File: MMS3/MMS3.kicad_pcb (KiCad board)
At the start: 4 copper layers, 100 x 50 mm, 198 parts, among them J1 86093488324755V1LF, J2 AMASS XT60, J3 Programming header, J7 AMASS XT60, J8 RJ45_LED_Shielded, J800 USB_C_Receptacle_USB2.0_16P, J9 RJ45_LED_Shielded, Q700 MMST3904, SW3 TC-6615Z-12.5-260, SW4 SK12D07VG5, SW5 TC-6615Z-12.5-260, U1 STM32F405RGTx, U15 AMS1117-3.3, U2 TPS54560BDDA, U302 CH334P, U4 TPD2EUSB30DRTR-TP, U401 TPD2EUSB30DRTR-TP, U5 TPD2EUSB30DRTR-TP, U500 TJA1044GTK_3Z, U501 TJA1044GTK_3Z, U6 AT24C256C, U700 STM32F103CBTx, U801 FSUSB42UMX, U802 FSUSB42UMX, X1 X32258MOB4SI, X2 Q13FC1350000400, Y700 Crystal_GND24, Y900 Crystal_GND24

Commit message: initial PCB update
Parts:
- removed C21, C22, C23, C25, C26, C312, C313, C701, C702, C703, C704, C705, C706, C800, C900: 100nF, PCM_JLCPCB:C_0402
- removed C24: 10uF, PCM_JLCPCB:C_0603
- removed C28, C29: 33pF, PCM_JLCPCB:C_0402
- removed C30, C31, C32, C33, C34: 10uF, PCM_JLCPCB:C_0805
- removed C7: 10nF, PCM_JLCPCB:C_0402
- removed C700, C904: 1uF, PCM_JLCPCB:C_0402
- removed C8: 18pF, PCM_JLCPCB:C_0402
- removed C902: 10uF, PCM_JLCPCB:C_0402
- removed D301, D700, D701: Red, PCM_JLCPCB:D_0603
- removed FB401: ~, PCM_JLCPCB:FB_0603
- removed J800: USB_C_Receptacle_USB2.0_16P, Connector_USB:USB_C_Receptacle_GCT_USB4105-xx-A_16P_TopMnt_Horizontal
- removed LED1: FixLed307, FixLed307:FixLed307
- removed Q700: MMST3904, Package_TO_SOT_SMD:SOT-23
- removed R27, R308, R31, R40: 1kΩ, PCM_JLCPCB:R_0402
- removed R500, R701, R703, R705, R706, R709, R802, R804, R805, R807: 10kΩ, PCM_JLCPCB:R_0402
- removed R700, R702: 100kΩ, PCM_JLCPCB:R_0402
- removed R704, R708, R715, R716, R902, R903, R906, R907: 22Ω, PCM_JLCPCB:R_0402
- removed R707, R713: 220Ω, PCM_JLCPCB:R_0402
- removed R710, R714: 100Ω, PCM_JLCPCB:R_0402
- removed R711: 24.9kΩ, PCM_JLCPCB:R_0402
- removed R712: 1.5kΩ, PCM_JLCPCB:R_0402
- removed R803, R806: 22kΩ, PCM_JLCPCB:R_0402
- removed REF**: WEEE-Logo_4.2x6mm_SilkScreen, Symbol:WEEE-Logo_4.2x6mm_SilkScreen
- removed SW3, SW5: TC-6615Z-12.5-260, Tact-sw:SW-TH_4P-L7.3-TC-6615Z-12.5-260
- removed SW4: SK12D07VG5, Slide-SW:SW-TH_SK12D07VG5-1
- removed TP10, TP11, TP12, TP13, TP14, TP5, TP7, TP8, TP9: TestPoint, TestPoint:TestPoint_Pad_D1.0mm
- removed U302: CH334P, Package_DFN_QFN:QFN-16-1EP_3x3mm_P0.5mm_EP1.7x1.7mm
- removed U401: TPD2EUSB30DRTR-TP, Package_TO_SOT_SMD:SOT-723
- removed U500: TJA1044GTK_3Z, Package_SON:HVSON-8-1EP_3x3mm_P0.65mm_EP1.6x2.4mm
- removed U700: STM32F103CBTx, Package_QFP:LQFP-48_7x7mm_P0.5mm
- removed U801, U802: FSUSB42UMX, Package_DFN_QFN:UQFN-10_1.4x1.8mm_P0.4mm
- removed X2: Q13FC1350000400, PCM_JLCPCB:FC-135R_L3.2-W1.5
- removed Y700: Crystal_GND24, PCM_JLCPCB:CRYSTAL-SMD_4P-L3.2-W2.5-BL
- removed Y900: Crystal_GND24, Crystal:Crystal_SMD_3225-4Pin_3.2x2.5mm
- added C14: 10nF, PCM_JLCPCB:C_0402, F.Cu at (152.4, 154.4)
- added C48: 22uF, PCM_JLCPCB:C_0805, F.Cu at (139.2, 166.7)
- added C51: 22uF, PCM_JLCPCB:C_0805, F.Cu at (139.2, 169.7)
- added C64: 100uF, Capacitor_SMD:CP_Elec_10x10, F.Cu at (130.6, 149.4)
- added D10: SS510B, PCM_JLCPCB:D_SMB, F.Cu at (141.6, 151.8)
- added D2: SMF58CA, PCM_JLCPCB:D_SOD-123FL, F.Cu at (139.8, 163.5)
- added D7: SS510B, PCM_JLCPCB:D_SMB, F.Cu at (141.6, 146.3)
- added D8: Red, PCM_JLCPCB:D_0603, F.Cu at (139.4, 155.9)
- added D9: Red, PCM_JLCPCB:D_0603, F.Cu at (139.4, 158.5)
- added J4: USB_C_Receptacle_USB2.0_16P, Connector_USB:USB_C_Receptacle_GCT_USB4105-xx-A_16P_TopMnt_Horizontal, F.Cu at (153.6, 148.8)
- added J5: USB_PD, Connector_USB:USB_C_Receptacle_GCT_USB4105-xx-A_16P_TopMnt_Horizontal, F.Cu at (129.1, 167.1)
- added Q1: MMBT5401 200-300, PCM_JLCPCB:Q_SOT-23, F.Cu at (146.9, 168.7)
- added Q2: DOINGTER DON50N10-TL, CMSA160N10:PDFN-8_L5.8-W5.0-P1.27-LS6.1-BL, F.Cu at (157.1, 176.9)
- added Q3: DOINGTER DON50N10-TL, CMSA160N10:PDFN-8_L5.8-W5.0-P1.27-LS6.1-BL, F.Cu at (148.2, 176.9)
- added S1: Tactile Button, 160gf, PCM_JLCPCB:SW_TS-1088-AR02016, F.Cu at (148.0, 164.0)
- added S2: Tactile Button, 160gf, PCM_JLCPCB:SW_TS-1088-AR02016, F.Cu at (157.1, 164.0)
- added S3: Tactile Button, 160gf, PCM_JLCPCB:SW_TS-1088-AR02016, F.Cu at (157.1, 168.5)
- added U3: TPD2EUSB30DRTR-TP, Package_TO_SOT_SMD:SOT-723, F.Cu at (149.6, 154.9)
- added U7: MX74502D23_C41433189, MX74502D23:UDFN-8L_L2.0-W3.0-P0.50-BL-EP, F.Cu at (143.4, 156.9)
- C10, C11: value 22pF -> 100nF; footprint PCM_JLCPCB:C_0402 -> PCM_JLCPCB:C_0603
- C12, C13: footprint PCM_JLCPCB:C_0402 -> PCM_JLCPCB:C_0603
- C16: value 2.2uF -> 100nF; footprint PCM_JLCPCB:C_0402 -> PCM_JLCPCB:C_0603
- C17: value 2.2uF -> 1uF; footprint PCM_JLCPCB:C_0402 -> PCM_JLCPCB:C_0603
- C18: value 4.7nF -> 22uF; footprint PCM_JLCPCB:C_0402 -> PCM_JLCPCB:C_0805
- C19: value 100nF -> 100uF; footprint PCM_JLCPCB:C_0402 -> Capacitor_SMD:CP_Elec_10x10
- C3, C5: value 100nF -> 12pF; footprint PCM_JLCPCB:C_0402 -> PCM_JLCPCB:C_0603
- C36, C37: footprint PCM_JLCPCB:C_0402 -> PCM_JLCPCB:C_0805
- C38, C39: value 220nF -> 10uF
- C40: value 100nF -> 10uF
- C41, C42: value 22uF -> 220nF
- C45: value 22uF -> 100nF
- C50: value 100uF -> 22uF; footprint Capacitor_SMD:CP_Elec_10x10 -> PCM_JLCPCB:C_0805
- C9: value 18pF -> 100nF; footprint PCM_JLCPCB:C_0402 -> PCM_JLCPCB:C_0603
- D1: value SMF58CA -> Red; footprint PCM_JLCPCB:D_SOD-123FL -> PCM_JLCPCB:D_0603
- D4: value SS510B -> Red; footprint PCM_JLCPCB:D_SMB -> PCM_JLCPCB:D_0603
- J3: value Programming header -> WCH Link; footprint Connector_PinHeader_1.27mm:PinHeader_1x06_P1.27mm_Vertical -> Connector_PinSocket_2.54mm:PinSocket_2x05_P2.54mm_Vertical
- R10: footprint PCM_JLCPCB:R_0402 -> PCM_JLCPCB:R_0603
- R11: value 1kΩ -> 10kΩ; footprint PCM_JLCPCB:R_0402 -> PCM_JLCPCB:R_0603
- R12, R13: value 100Ω -> 1kΩ; footprint PCM_JLCPCB:R_0402 -> PCM_JLCPCB:R_0603
- R14: value 10kΩ -> 33kΩ
- R15: value 10kΩ -> 39kΩ; footprint PCM_JLCPCB:R_0402 -> PCM_JLCPCB:R_0603
- R16: value 22Ω -> 12kΩ; footprint PCM_JLCPCB:R_0402 -> PCM_JLCPCB:R_0603
- R17: value 22Ω -> 4.7kΩ; footprint PCM_JLCPCB:R_0402 -> PCM_JLCPCB:R_0603
- R18: value 22Ω -> 1kΩ; footprint PCM_JLCPCB:R_0402 -> PCM_JLCPCB:R_0603
- R19: value 22Ω -> 47kΩ; footprint PCM_JLCPCB:R_0402 -> PCM_JLCPCB:R_0603
- R20: value 22Ω -> 18kΩ; footprint PCM_JLCPCB:R_0402 -> PCM_JLCPCB:R_0603
- R21: value 22Ω -> 5.1kΩ; footprint PCM_JLCPCB:R_0402 -> PCM_JLCPCB:R_0603
- R22: value 100Ω -> 5.1kΩ; footprint PCM_JLCPCB:R_0402 -> PCM_JLCPCB:R_0603
- R7: value 33kΩ -> 10kΩ
- R8: value 5.1kΩ -> 1.5kΩ; footprint PCM_JLCPCB:R_0402 -> PCM_JLCPCB:R_0603
- R9: value 5.1kΩ -> 1kΩ; footprint PCM_JLCPCB:R_0402 -> PCM_JLCPCB:R_0603
- U1: value STM32F405RGTx -> CH32L103C8T6_C22398291; footprint Package_QFP:LQFP-64_10x10mm_P0.5mm -> CH32L103C8T6:LQFP-48_L7.0-W7.0-P0.50-LS9.0-BL
- X1: value X32258MOB4SI -> X322525MOB4SI
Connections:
- net /CAN_TR1/CAN.+ renamed /MMS_CONNECTOR_DOWNSTREAM/CAN1.+
- net /CAN_TR1/CAN.- renamed /MMS_CONNECTOR_DOWNSTREAM/CAN1.-
- C10 pad 1: /MCU/OSC_HSI_IN -> +3V3
- C11 pad 1: /MCU/OSC_HSI_OUT -> +3V3
- C12 pad 1: Net-(U1-NRST) -> +3V3
- C15 pad 1: /MCU/VDDA -> /USB_Data/VBUS
- C16 pad 1: Net-(U1-VCAP_1) -> BRD_VIN
- C17 pad 1: Net-(U1-VCAP_2) -> BRD_VIN
- C17 pad 2: GND -> Net-(U7-VCAP)
- C18 pad 1: /MCU/BOOT0 -> /PSU/NMos1/D
- C19 pad 1: +3V3 -> +5V
- C20 pad 1: +3V3 -> BRD_VIN
- C3 pad 1: +3V3 -> GND
- C3 pad 2: GND -> /CH32L103_Wrapper/CH32L103/OSC_IN
- C35 pad 1: /VRM/Cap_protec -> BRD_VIN
- C35 pad 2: GND -> /PSU/Buck Converter/Cap_protec
- C36 pad 1: /MCU/VDDA -> /PSU/Buck Converter/Cap_protec
- C37 pad 1: +3V3 -> BRD_VIN
- C37 pad 2: GND -> /PSU/Buck Converter/Cap_protec
- C38 pad 1: BRD_VIN -> /PSU/Buck Converter/Cap_protec
- C38 pad 2: /VRM/Cap_protec -> GND
- C39 pad 1: /VRM/Cap_protec -> BRD_VIN
- C39 pad 2: GND -> /PSU/Buck Converter/Cap_protec
- C40 pad 1: Net-(U2-SW) -> /PSU/Buck Converter/Cap_protec
- C40 pad 2: Net-(U2-BOOT) -> GND
- C41 pad 1: Net-(C41-Pad1) -> BRD_VIN
- C41 pad 2: GND -> /PSU/Buck Converter/Cap_protec
- C42 pad 1: Net-(C41-Pad1) -> /PSU/Buck Converter/Cap_protec
- C45 pad 1: Net-(C41-Pad1) -> Net-(U2-SW)
- C45 pad 2: GND -> Net-(U2-BOOT)
- C46 pad 1: Net-(C41-Pad1) -> /PSU/Buck Converter/5V out
- C47 pad 1: Net-(C41-Pad1) -> /PSU/Buck Converter/5V out
- C5 pad 2: +5V -> /CH32L103_Wrapper/CH32L103/OSC_Out
- C50 pad 1: +5V -> /PSU/Buck Converter/5V out
- C9 pad 1: /MCU/OSC32_OUT -> +3V3
- D1 pad 1: BRD_VIN -> Net-(D1-Pad1)
- D1 pad 2: GND -> /CH32L103_Wrapper/CH32L103/UART1.TX
- D4 pad 1: +5V -> /CH32L103_Wrapper/Chainbus_addr3
- D4 pad 2: Net-(C41-Pad1) -> Net-(D4-Pad2)
- D5 pad 2: VBUS -> /USB_Data/VBUS
- D6 pad 1: Net-(D6-Pad1) -> /CH32L103_Wrapper/PC13
- D6 pad 2: /Slide-SW/SEL -> Net-(D6-Pad2)
- J1 pad b1: /Interboard_connector/Chainbus_addr3 -> /CH32L103_Wrapper/Chainbus_addr3
- J1 pad b10: /I2C_Flash/I2C_Memory.SCL -> /CH32L103_Wrapper/I2C2.SCL
- J1 pad b11: /Interboard_connector/Chainbus.CS -> /CH32L103_Wrapper/SPI2.CS
- J1 pad b12: /Interboard_connector/Chainbus.SCK -> /CH32L103_Wrapper/SPI2.SCK
- J1 pad b13: /Interboard_connector/Chainbus.MOSI -> /CH32L103_Wrapper/SPI2.MOSI
- J1 pad b14: /Interboard_connector/Chainbus.MISO -> /CH32L103_Wrapper/SPI2.MISO
- J1 pad b15: /Interboard_connector/Chainbus.RX -> /CH32L103_Wrapper/UART4.RX
- J1 pad b16: /Interboard_connector/Chainbus.TX -> /CH32L103_Wrapper/UART4.TX
- J1 pad b2: /Interboard_connector/Chainbus_addr4 -> /CH32L103_Wrapper/Chainbus_addr4
- J1 pad b3: /Interboard_connector/Chainbus_addr0 -> /CH32L103_Wrapper/Chainbus_addr0
- J1 pad b4: /Interboard_connector/Chainbus_addr1 -> /CH32L103_Wrapper/Chainbus_addr1
- J1 pad b5: /Interboard_connector/Chainbus_addr2 -> /CH32L103_Wrapper/Chainbus_addr2
- J1 pad b6: /Interboard_connector/Chainbus_addr5 -> /CH32L103_Wrapper/Chainbus_addr5
- J1 pad b7: /Interboard_connector/Chainbus_addr6 -> /CH32L103_Wrapper/Chainbus_addr6
- J1 pad b8: /Interboard_connector/Chainbus_addr7 -> /CH32L103_Wrapper/Chainbus_addr7
- J1 pad b9: /I2C_Flash/I2C_Memory.SDA -> /CH32L103_Wrapper/I2C2.SDA
- J3 pad 1: +3V3 -> /CH32L103_Wrapper/CH32L103/UART1.TX
- J3 pad 2: /STlink-BMprobe/DIO -> /CH32L103_Wrapper/CH32L103/PA14 (SWCLK)
- J3 pad 3: /STlink-BMprobe/CLK -> /CH32L103_Wrapper/CH32L103/UART1.RX
- J3 pad 4: /STlink-BMprobe/STLINK-RST -> /CH32L103_Wrapper/CH32L103/PA13 (SWDIO)
- J3 pad 5: GND -> unconnected-(J3-Pin_5-Pad5)
- J3 pad 6: /STlink-BMprobe/STLINK-BOOT0 -> GND
- J9 pad 7: /MMS_CONNECTOR_UPSTREAM/USB_MMS_CONN.D- -> /MMS_CONNECTOR_DOWNSTREAM/USB_MMS_CONN.D-
- J9 pad 8: /MMS_CONNECTOR_UPSTREAM/USB_MMS_CONN.D+ -> /MMS_CONNECTOR_DOWNSTREAM/USB_MMS_CONN.D+
- L1 pad 2: Net-(C41-Pad1) -> /PSU/Buck Converter/5V out
- R1 pad 2: /MCU/USER_LED_2 -> /TXD2_LED
- R10 pad 1: /MCU/BOOT0 -> /CH32L103_Wrapper/CH32L103/BOOT0
- R11 pad 1: /MCU/BOOT_EN -> /CH32L103_Wrapper/CH32L103/~{RST}
- R11 pad 2: /MCU/BOOT0 -> +3V3
- R12 pad 1: /MCU/NRST -> Net-(D4-Pad2)
- R12 pad 2: /MCU/SWD.~{RST} -> GND
- R13 pad 1: /MCU/USR_BTN -> Net-(D6-Pad2)
- R13 pad 2: /MCU/USR_BUTTON -> GND
- R14 pad 1: /MCU/USR_BTN -> Net-(J4-SHIELD)
- R14 pad 2: +3V3 -> GND
- R15 pad 1: /MCU/NRST -> BRD_VIN
- R15 pad 2: +3V3 -> /PSU/EN
- R16 pad 1: /USB HUB/USBIN1_R.D+ -> /PSU/EN
- R16 pad 2: /USB HUB/USBIN1.D+ -> GND
- R17 pad 1: /USB HUB/USBIN1_R.D- -> Net-(D8-Pad1)
- R17 pad 2: /USB HUB/USBIN1.D- -> GND
- R18 pad 1: /USB HUB/USBBYP.D+ -> Net-(D9-Pad1)
- R18 pad 2: /USB HUB/USBIN1.D+ -> GND
- R19 pad 1: /USB HUB/USBBYP.D- -> BRD_VIN
- R19 pad 2: /USB HUB/USBIN1.D- -> Net-(U7-OV)
- R20 pad 1: /USB HUB/USBBYP.D- -> Net-(U7-OV)
- R20 pad 2: /MCU/USB_MCU.D- -> GND
- R21 pad 1: /USB HUB/USBBYP.D+ -> /CH32L103_Wrapper/CH32L103/I2C1.SDA
- R21 pad 2: /MCU/USB_MCU.D+ -> GND
- R22 pad 1: /MCU/NRST -> /CH32L103_Wrapper/CH32L103/I2C1.SCL
- R22 pad 2: Net-(U1-NRST) -> GND
- R33 pad 2: /VRM/Cap_protec -> /PSU/Buck Converter/Cap_protec
- R34 pad 1: /VRM/Cap_protec -> /PSU/Buck Converter/Cap_protec
- R36 pad 1: Net-(C41-Pad1) -> /PSU/Buck Converter/5V out
- R4 pad 2: /MCU/USER_LED_1 -> /RXD2_LED
- R7 pad 1: Net-(J800-SHIELD) -> /CH32L103_Wrapper/CH32L103/UART1.RX
- R8 pad 1: /USBC_CONN/CC2 -> /CH32L103_Wrapper/PC13
- R8 pad 2: GND -> Net-(Q1-B)
- R9 pad 1: /USBC_CONN/CC1 -> Net-(D1-Pad1)
- TP1 pad 1: /CAN_TR1/CAN.TX -> /CAN_TR2/CAN.RX
- TP19 pad 1: Net-(C41-Pad1) -> /PSU/Buck Converter/5V out
- TP3 pad 1: /CAN_TR1/CAN.RX -> /CAN_TR2/CAN.TX
- U1 pad 10: /Interboard_connector/Altmode14 -> /CH32L103_Wrapper/Chainbus_addr3
- U1 pad 11: /Interboard_connector/Altmode15 -> /CH32L103_Wrapper/Chainbus_addr4
- U1 pad 12: GND -> /CH32L103_Wrapper/Chainbus_addr0
- U1 pad 13: /MCU/VDDA -> /CH32L103_Wrapper/Chainbus_addr1
- U1 pad 14: /Interboard_connector/Altmode7 -> /CH32L103_Wrapper/Chainbus_addr2
- U1 pad 15: /Interboard_connector/Altmode8 -> /CH32L103_Wrapper/Chainbus_addr5
- U1 pad 16: /Interboard_connector/Altmode9 -> /CH32L103_Wrapper/Chainbus_addr6
- U1 pad 17: /Interboard_connector/Altmode10 -> /CH32L103_Wrapper/Chainbus_addr7
- U1 pad 18: GND -> /CH32L103_Wrapper/UART4.TX
- U1 pad 19: +3V3 -> /CH32L103_Wrapper/UART4.RX
- U1 pad 2: unconnected-(U1-PC13-Pad2) -> /CH32L103_Wrapper/PC13
- U1 pad 20: /MCU/BOOT_EN -> /TXD2_LED
- U1 pad 21: /Interboard_connector/Chainbus_addr2 -> /CH32L103_Wrapper/I2C2.SDA
- U1 pad 22: /Interboard_connector/Chainbus_addr1 -> /CH32L103_Wrapper/I2C2.SCL
- U1 pad 23: /Interboard_connector/Chainbus_addr0 -> GND
- U1 pad 24: /Interboard_connector/Altmode16 -> +3V3
- U1 pad 25: /MCU/USER_LED_3 -> /CH32L103_Wrapper/SPI2.CS
- U1 pad 26: /MCU/USER_LED_2 -> /CH32L103_Wrapper/SPI2.SCK
- U1 pad 27: /MCU/USER_LED_1 -> /CH32L103_Wrapper/SPI2.MOSI
- U1 pad 28: unconnected-(U1-PB2-Pad28) -> /CH32L103_Wrapper/SPI2.MISO
- U1 pad 29: /I2C_Flash/I2C_Memory.SCL -> /CH32L103_Wrapper/CH32L103/PA8
- U1 pad 3: /MCU/OSC32_IN -> /CH32L103_Wrapper/CH32L103/PC14 (OSC32)
- U1 pad 30: /I2C_Flash/I2C_Memory.SDA -> /CH32L103_Wrapper/CH32L103/UART1.TX
- U1 pad 31: Net-(U1-VCAP_1) -> /CH32L103_Wrapper/CH32L103/UART1.RX
- U1 pad 32: +3V3 -> /CH32L103_Wrapper/USB1.D-
- U1 pad 33: /CAN_TR2/CAN.RX -> /CH32L103_Wrapper/USB1.D+
- U1 pad 34: /Interboard_connector/Altmode4 -> /CH32L103_Wrapper/CH32L103/PA13 (SWDIO)
- U1 pad 35: /Interboard_connector/Altmode5 -> GND
- U1 pad 36: /Interboard_connector/Altmode6 -> +3V3
- U1 pad 37: /Interboard_connector/Chainbus_addr5 -> /CH32L103_Wrapper/CH32L103/PA14 (SWCLK)
- U1 pad 38: /Interboard_connector/Chainbus_addr6 -> /CH32L103_Wrapper/CH32L103/PA15
- U1 pad 39: /Interboard_connector/Chainbus_addr7 -> /CH32L103_Wrapper/CH32L103/PB3
- U1 pad 4: /MCU/OSC32_OUT -> /CH32L103_Wrapper/CH32L103/PC15 (OSC32)
- U1 pad 40: /Interboard_connector/Chainbus_addr3 -> /CH32L103_Wrapper/CH32L103/PB4
- U1 pad 41: /Interboard_connector/Altmode1 -> /CH32L103_Wrapper/CH32L103/PB5
- U1 pad 42: /Interboard_connector/Altmode2 -> /CH32L103_Wrapper/CH32L103/I2C1.SCL
- U1 pad 43: /Interboard_connector/Altmode3 -> /CH32L103_Wrapper/CH32L103/I2C1.SDA
- U1 pad 44: /MCU/USB_MCU.D- -> /CH32L103_Wrapper/CH32L103/BOOT0
- U1 pad 45: /MCU/USB_MCU.D+ -> /CAN_TR2/CAN.RX
- U1 pad 46: /MCU/SWD.SWDIO -> /CAN_TR2/CAN.TX
- U1 pad 47: Net-(U1-VCAP_2) -> GND
- U1 pad 5: /MCU/OSC_HSI_IN -> /CH32L103_Wrapper/CH32L103/OSC_IN
- U1 pad 6: /MCU/OSC_HSI_OUT -> /CH32L103_Wrapper/CH32L103/OSC_Out
- U1 pad 7: Net-(U1-NRST) -> /CH32L103_Wrapper/CH32L103/~{RST}
- U1 pad 8: /Interboard_connector/Altmode12 -> GND
- U1 pad 9: /Interboard_connector/Altmode13 -> +3V3
- U5 pad 1: /MMS_CONNECTOR_UPSTREAM/USB_MMS_CONN.D- -> /MMS_CONNECTOR_DOWNSTREAM/USB_MMS_CONN.D-
- U5 pad 2: /MMS_CONNECTOR_UPSTREAM/USB_MMS_CONN.D+ -> /MMS_CONNECTOR_DOWNSTREAM/USB_MMS_CONN.D+
- U6 pad 5: /I2C_Flash/I2C_Memory.SDA -> /CH32L103_Wrapper/I2C2.SDA
- U6 pad 6: /I2C_Flash/I2C_Memory.SCL -> /CH32L103_Wrapper/I2C2.SCL
- X1 pad 1: /MCU/OSC_HSI_OUT -> /CH32L103_Wrapper/CH32L103/OSC_IN
- X1 pad 3: /MCU/OSC_HSI_IN -> /CH32L103_Wrapper/CH32L103/OSC_Out
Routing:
- net (no net): track 0.00 -> 311.8 mm, vias 0 -> 11
- net /MCU/SWD.SWDIO: track 58.0 -> 0.00 mm, vias 2 -> 0
- net /Slide-SW/SEL: track 54.3 -> 0.00 mm, vias 1 -> 0
- net +3V3: track 318.1 -> 370.6 mm, vias 49 -> 50
- net /Interboard_connector/Chainbus.SCK: track 49.0 -> 0.00 mm, vias 1 -> 0
- net /CH32L103_Wrapper/SPI2.SCK: track 0.00 -> 49.0 mm, vias 0 -> 1
- net /Interboard_connector/Chainbus.MISO: track 39.8 -> 0.00 mm, vias 1 -> 0
- net /CH32L103_Wrapper/SPI2.MISO: track 0.00 -> 39.8 mm, vias 0 -> 1
- net /Interboard_connector/Chainbus.TX: track 31.6 -> 0.00 mm, vias 1 -> 0
- net /CH32L103_Wrapper/UART4.TX: track 0.00 -> 31.6 mm, vias 0 -> 1
- net /Interboard_connector/Chainbus_addr3: track 27.9 -> 0.00 mm, vias 1 -> 0
- net /CH32L103_Wrapper/Chainbus_addr3: track 0.00 -> 27.9 mm, vias 0 -> 1
- net /USB switch1/USB_OUT2.D-: track 27.0 -> 0.00 mm
- net /USB switch1/USB_OUT2.D+: track 26.5 -> 0.00 mm
- net /Interboard_connector/Chainbus.CS: track 26.3 -> 0.00 mm, vias 1 -> 0
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- added copper zone on In2.Cu, net /CH32L103_Wrapper/Chainbus_addr1
- added copper zone on F.Cu, net /PSU/Buck Converter/5V out
- added copper zone on F.Cu, net /USB_Data/VBUS
- added copper zone on In2.Cu, net /USB_Data/VBUS
- removed copper zone on In2.Cu, net /MCU/VDDA
- removed copper zone on F.Cu, net /VRM/Cap_protec
- removed copper zone on F.Cu, net Net-(C41-Pad1)
- removed copper zone on F.Cu, net VBUS
- removed copper zone on In2.Cu, net VBUS

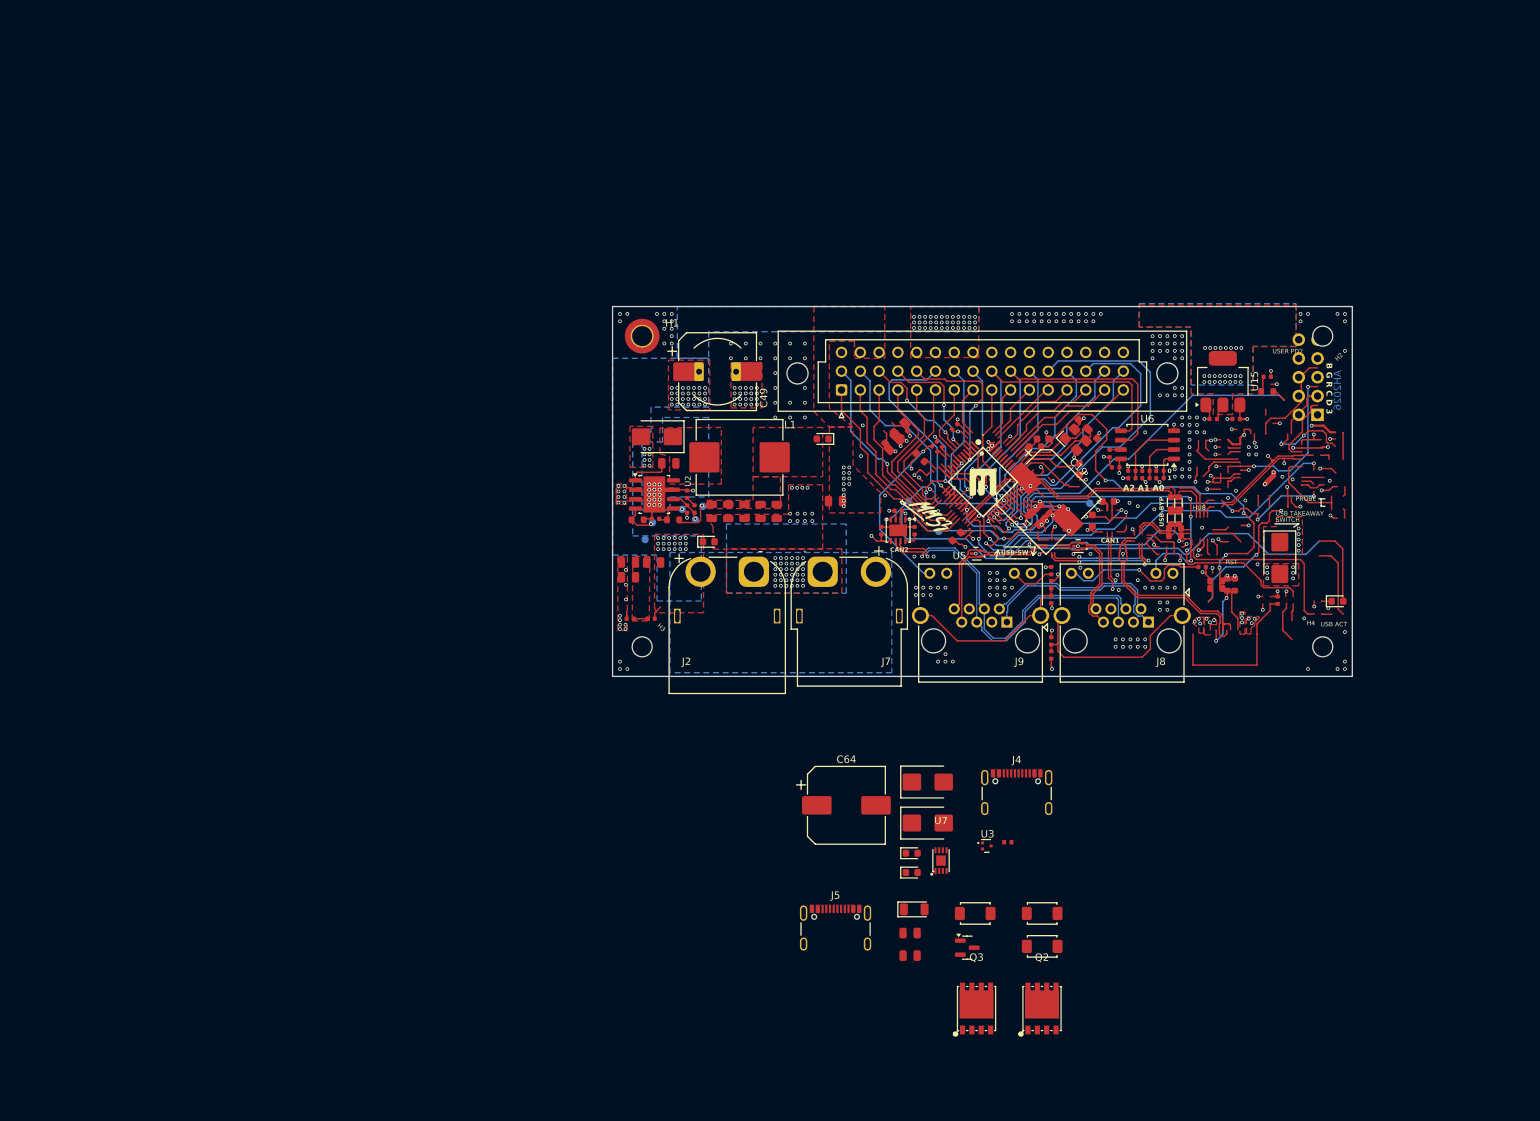
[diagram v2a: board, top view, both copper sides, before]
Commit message: re-added onboard programmer
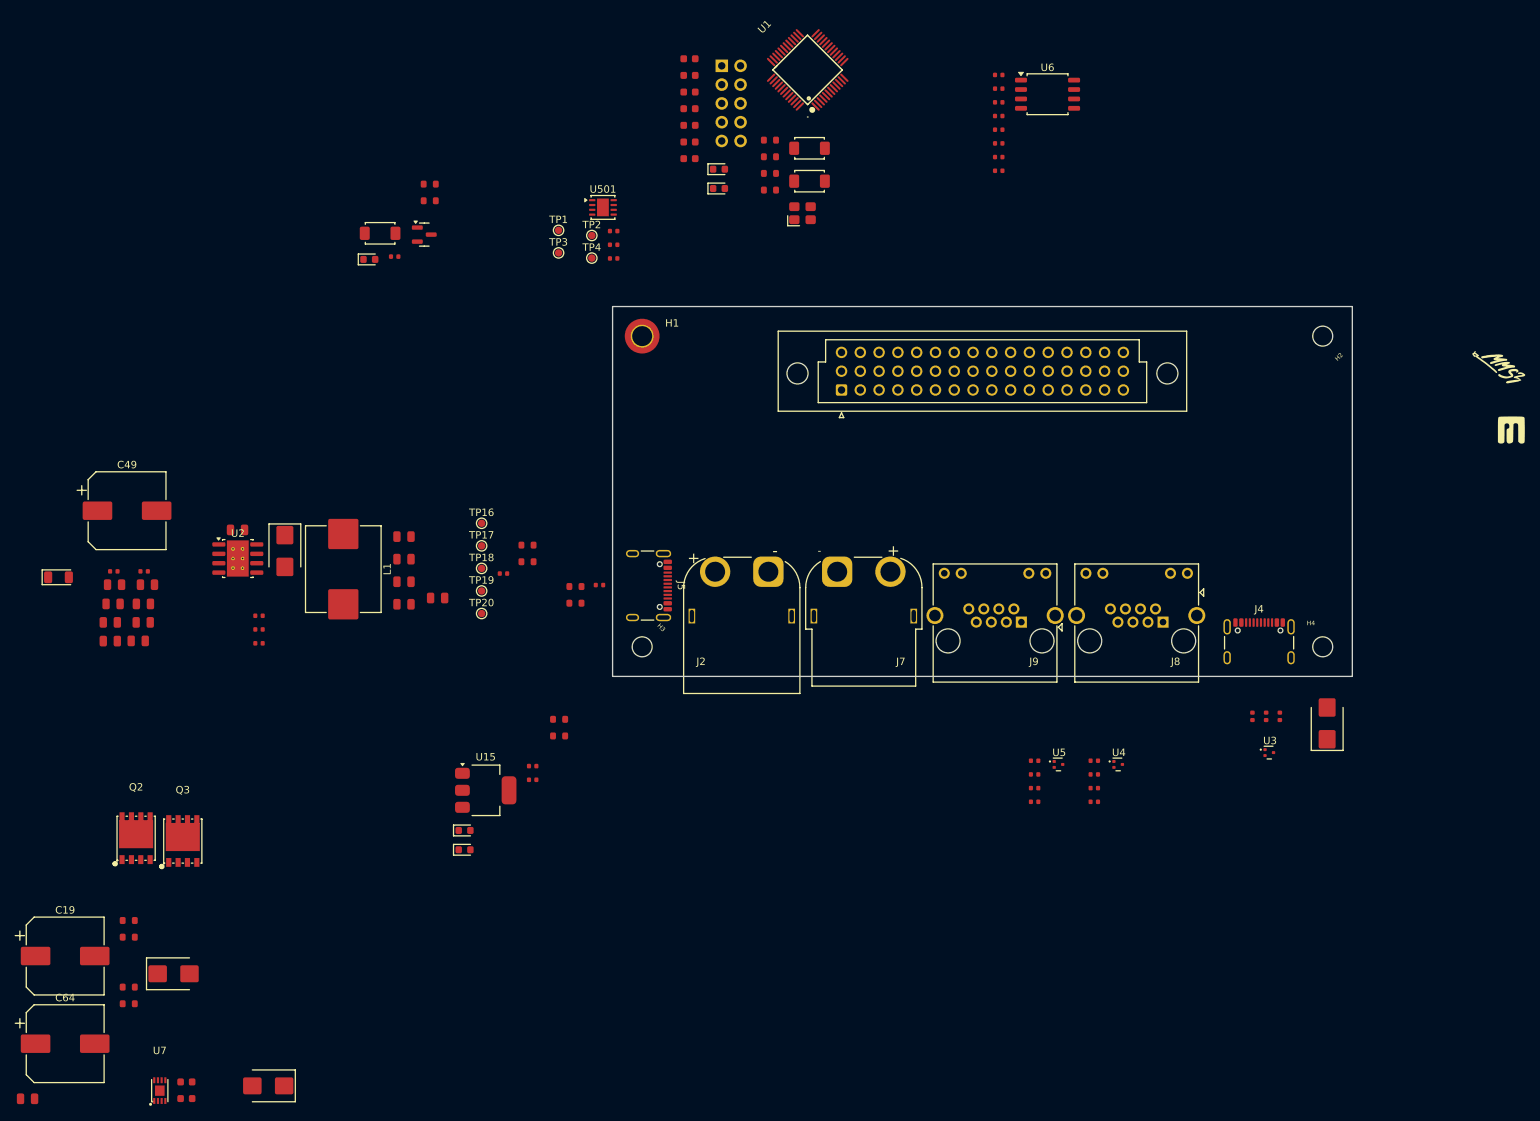
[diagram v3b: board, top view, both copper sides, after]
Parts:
- TP1, TP16, TP17, TP18, TP19, TP2, TP20, TP3, TP4: moved to F.Cu
- moved C18 157.2 mm to (19.9, 189.1), turned to 0 degrees
- moved R20 157.2 mm to (33.6, 176.2), turned to 0 degrees
- moved R19 154.5 mm to (33.6, 174.0), turned to 0 degrees
- moved R15 154.0 mm to (33.6, 165.0), turned to 0 degrees
- moved R16 151.5 mm to (33.6, 167.2), turned to 0 degrees
- moved C19 146.3 mm to (25.0, 169.8), turned to 0 degrees
- moved C16 130.3 mm to (41.4, 186.8), turned to 0 degrees
- moved C17 128.9 mm to (41.4, 189.1), turned to 0 degrees
- moved R7 128.1 mm to (69.5, 75.2), turned to 0 degrees
- moved Q2 124.6 mm to (34.6, 153.9)
- moved D2 124.1 mm to (24.1, 118.6)
- moved S1 122.2 mm to (67.6, 72.1)
- moved R8 121.5 mm to (74.3, 65.5), turned to 0 degrees
- moved Q1 121.2 mm to (73.5, 72.3)
- moved R9 119.7 mm to (74.3, 67.7), turned to 0 degrees
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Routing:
- net +3V3: track 370.6 -> 0.00 mm, vias 50 -> 0
- net (no net): track 311.8 -> 0.00 mm, vias 11 -> 0
- net +12V stby: track 152.1 -> 0.00 mm
- net GND: track 121.7 -> 0.00 mm, vias 369 -> 0
- net +5V: track 108.2 -> 0.00 mm, vias 24 -> 0
- net Net-(J8-~-Pad10): track 73.4 -> 0.00 mm, vias 5 -> 0
- net /MCU/USER_LED_3: track 73.4 -> 0.00 mm, vias 6 -> 0
- net /MCU/NRST: track 56.0 -> 0.00 mm, vias 4 -> 0
- net /MCU/SWD.SWCLK: track 54.6 -> 0.00 mm, vias 4 -> 0
- net /I2C_Flash/I2C_Memory.SCL: track 53.7 -> 0.00 mm, vias 1 -> 0
- net /I2C_Flash/I2C_Memory.SDA: track 50.0 -> 0.00 mm, vias 1 -> 0
- net /CH32L103_Wrapper/SPI2.SCK: track 49.0 -> 0.00 mm, vias 1 -> 0
- net /MCU/USR_BUTTON: track 48.4 -> 0.00 mm, vias 1 -> 0
- net /CAN_TR2/CAN.+: track 47.5 -> 0.00 mm, vias 1 -> 0
- net /CAN_TR2/CAN.-: track 47.1 -> 0.00 mm, vias 1 -> 0
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- removed copper zone on B.Cu, net +3V3
- removed copper zone on F.Cu, net +3V3
- removed copper zone on In2.Cu, net +3V3
- removed copper zone on F.Cu, net +5V
- removed copper zone on In2.Cu, net +5V
- removed copper zone on In2.Cu, net /CH32L103_Wrapper/Chainbus_addr1
- removed copper zone on F.Cu, net /PSU/Buck Converter/5V out
- removed copper zone on F.Cu, net /USB_Data/VBUS
- removed copper zone on In2.Cu, net /USB_Data/VBUS
- removed copper zone on B.Cu, net BRD_VIN
- removed copper zone on F.Cu, net BRD_VIN
- removed copper zone on B.Cu, net GND
- removed copper zone on F.Cu, net GND
- removed copper zone on F.Cu, net Net-(U2-SW)
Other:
- board text removed: "0 1"
- board text removed: "A2 A1 A0"
- board text removed: "AH2026"
- board text removed: "B G R C D 3"
- board text removed: "CAN1"
- board text removed: "CAN2"
- board text removed: "HUB"
- board text removed: "LINK PRG"
- board text removed: "PROBE"
- board text removed: "RST"
- board text removed: "SWITCH"
- board text removed: "USB ACT"
- board text removed: "USB TAKEAWAY"
- board text removed: "USB-BYP"
- board text removed: "USB-SW"
- board text removed: "USER PD2"
